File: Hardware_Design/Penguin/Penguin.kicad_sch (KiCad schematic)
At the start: 15 parts, among them SW1 SW_SPDT, U1 STM32F405RGT6

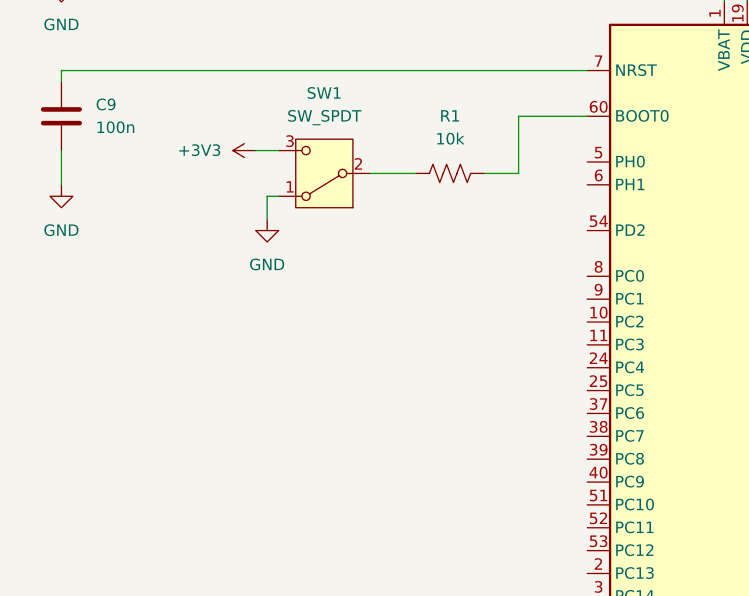
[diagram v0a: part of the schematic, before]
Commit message: Added Crystal Oscillator
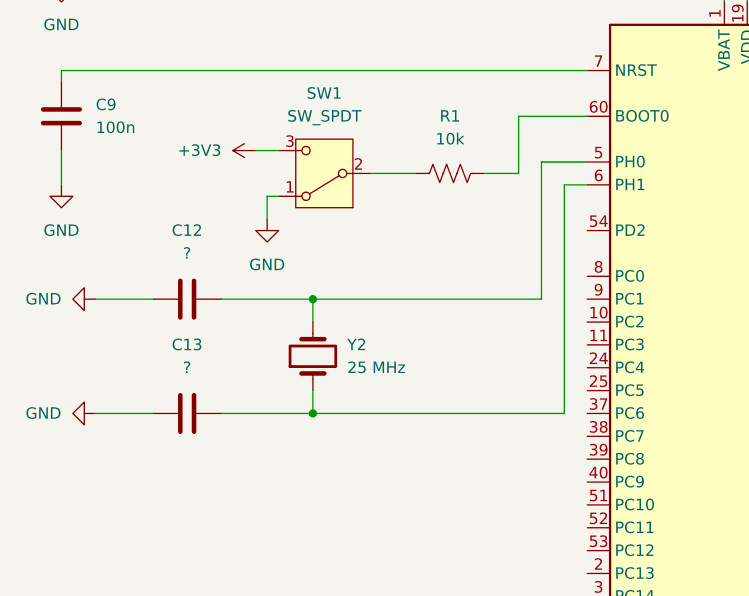
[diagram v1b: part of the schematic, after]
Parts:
- added C12, C13: ?, symbol Device:C
- added Y2: 25 MHz, symbol Device:Crystal
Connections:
- net GND: now also C12.1, C13.1
- net at U1.5 (PH0): now also C12.2, Y2.2
- net at U1.6 (PH1): now also C13.2, Y2.1

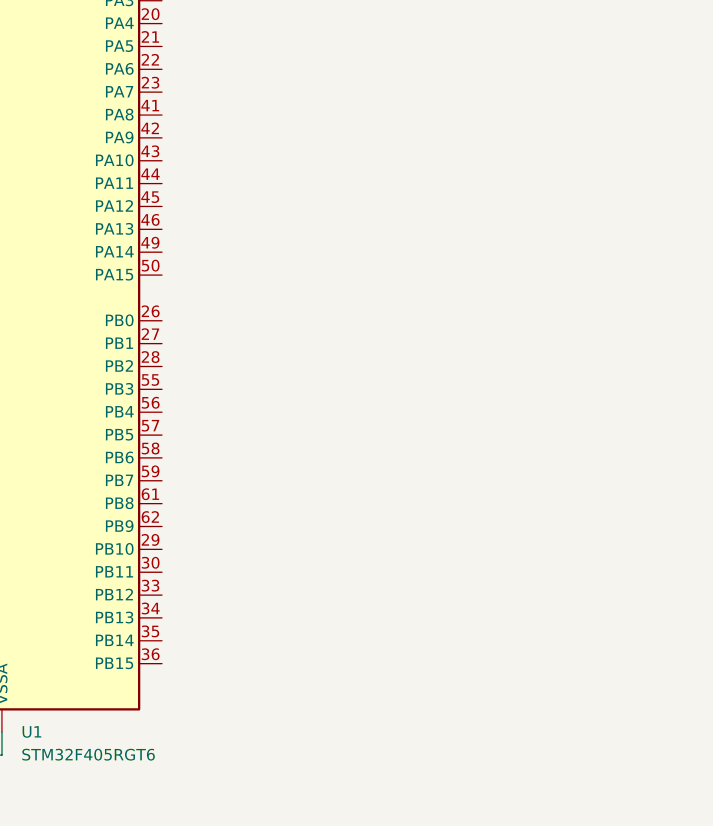
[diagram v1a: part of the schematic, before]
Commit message: Added Micro USB
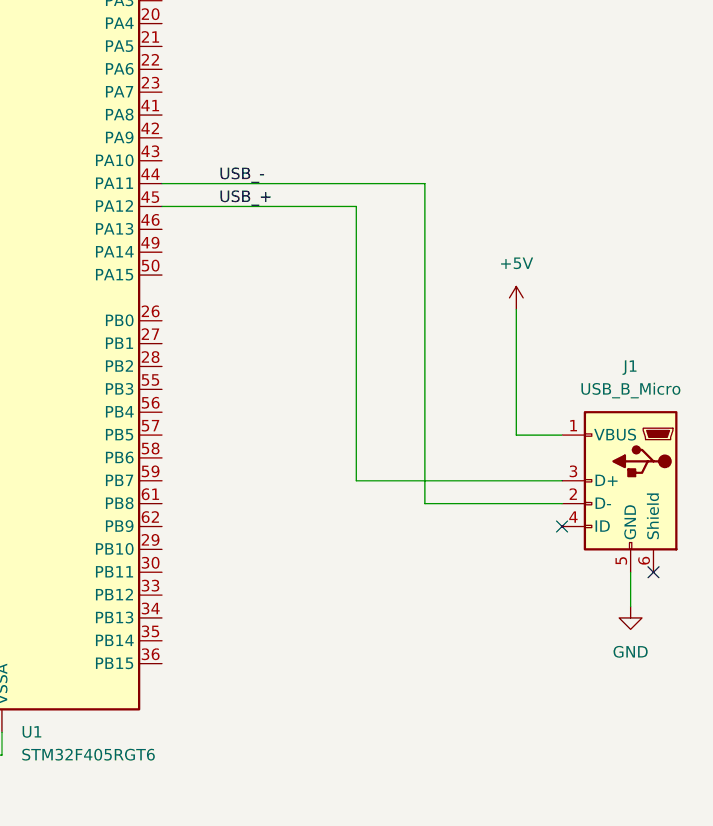
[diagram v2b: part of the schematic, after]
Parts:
- added J1: USB_B_Micro, symbol Connector:USB_B_Micro
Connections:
- net GND: now also J1.5 (GND)
- net USB_-: now reaches U1.44 (PA11)
- net USB_-: now also J1.2 (D-)
- net USB_+: now reaches U1.45 (PA12)
- net USB_+: now also J1.3 (D+)
- new net +5V: J1.1 (VBUS)
- no-connect marks 0 -> 2
